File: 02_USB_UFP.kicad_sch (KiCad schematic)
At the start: 36 parts, among them J1 USB_C_Receptacle, U5 TVS2200DRVx, U6 PI3USB302-Ax, U7 TUSB522Px

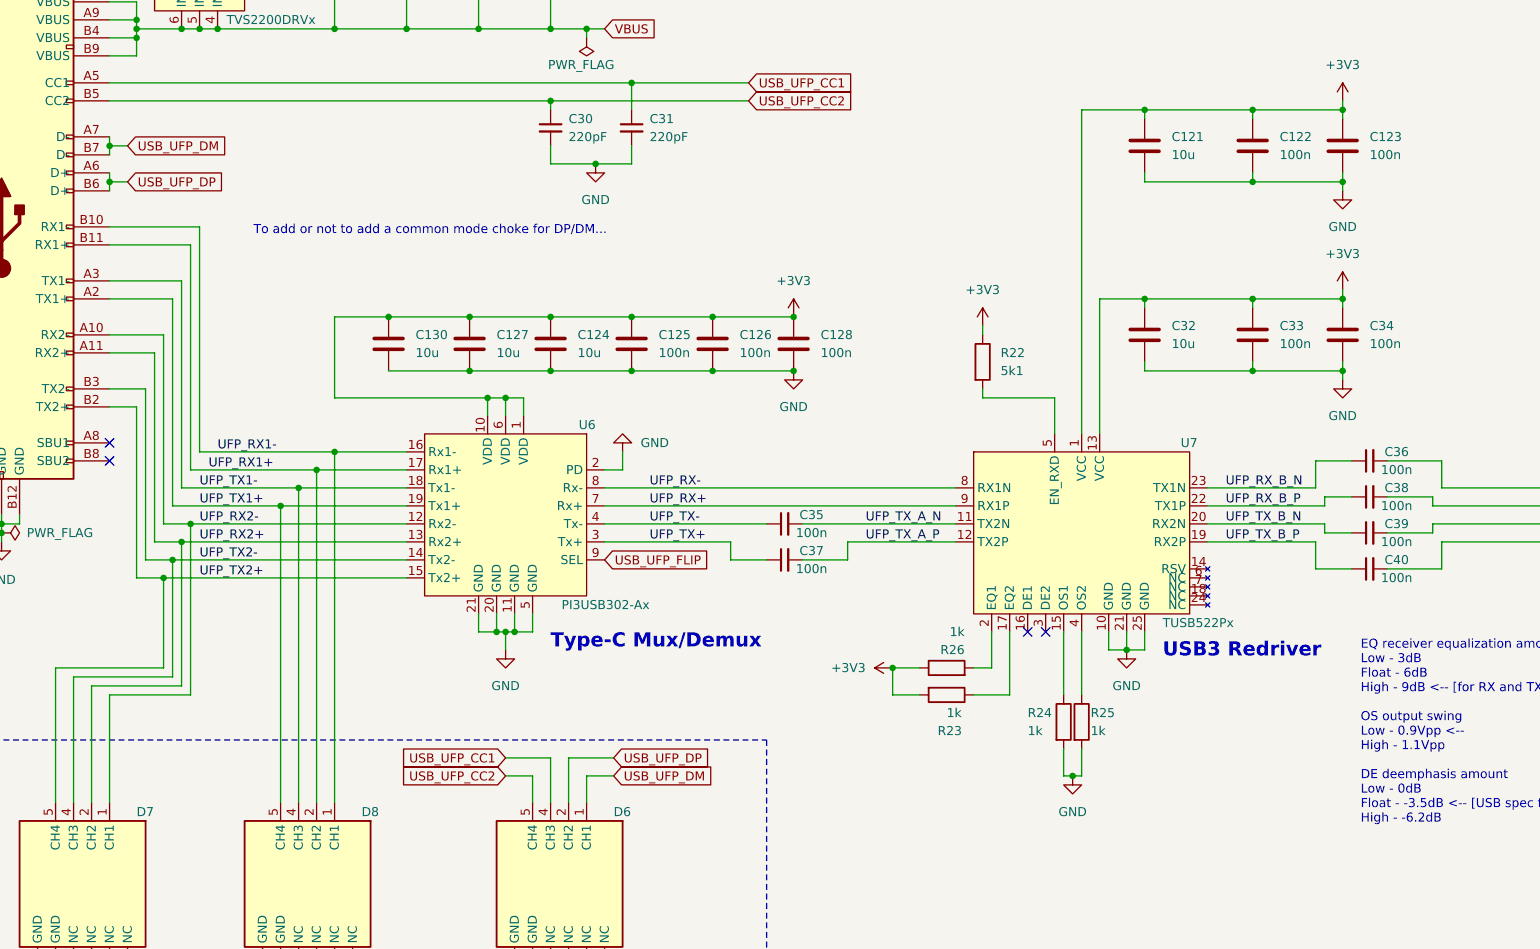
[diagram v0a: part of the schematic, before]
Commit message: route power delivery controller
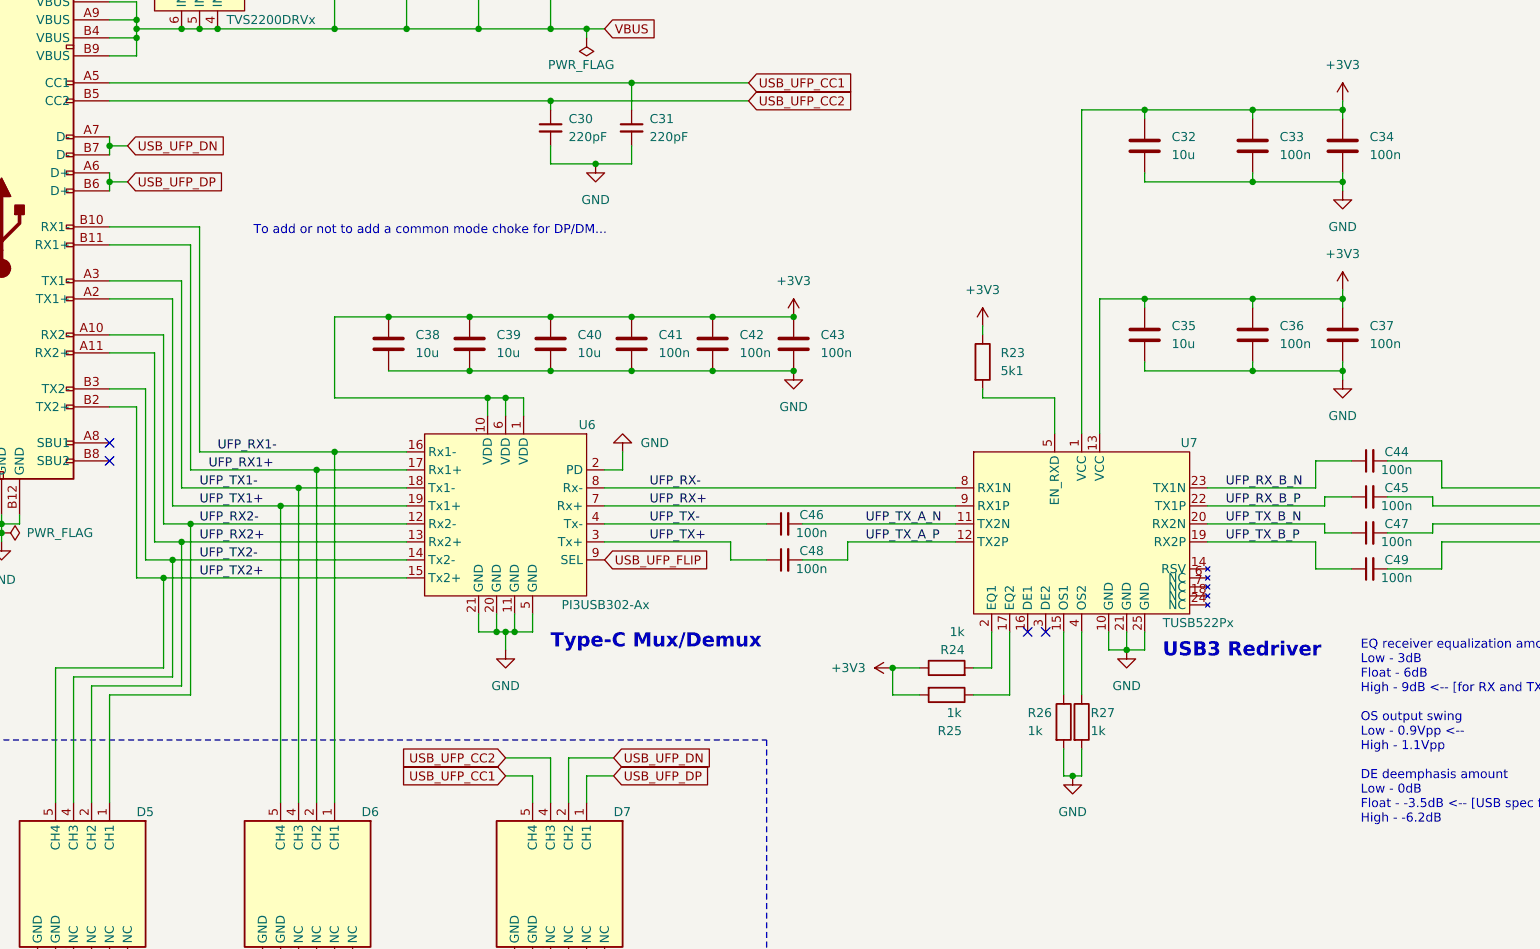
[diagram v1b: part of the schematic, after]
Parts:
- C26, C27, C28, C29: footprint Capacitor_SMD:C_0603_1608Metric -> Capacitor_SMD:C_0402_1005Metric
- renumbered C121 to C32, C122 to C33, C123 to C34, C32 to C35, C33 to C36, C34 to C37, C130 to C38, C127 to C39, C124 to C40, C125 to C41, C126 to C42, C128 to C43, C36 to C44, C38 to C45, C35 to C46, C39 to C47, C37 to C48, C40 to C49, D7 to D5, D8 to D6, D6 to D7, R22 to R23, R26 to R24, R23 to R25, R24 to R26, R25 to R27
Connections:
- net USB_UFP_CC1: now also D7.5 (CH4); no longer D7.4 (CH3)
- net USB_UFP_CC2: now also D7.4 (CH3); no longer D7.5 (CH4)
- net USB_UFP_DP: now also D7.1 (CH1); no longer D7.2 (CH2)
- net USB_UFP_DM renamed USB_UFP_DN
- net USB_UFP_DN: now also D7.2 (CH2); no longer D7.1 (CH1)

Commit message: settle on a layout
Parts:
- C30, C31, C33, C34, C36, C37, C41, C42, C43: footprint Capacitor_SMD:C_0603_1608Metric -> Capacitor_SMD:C_0402_1005Metric
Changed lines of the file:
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@@
       (effects (font (size 1.27 1.27)) (justify left))
     )
-    (property "Footprint" "Capacitor_SMD:C_0603_1608Metric" (at 152.0952 99.06 0)
+    (property "Footprint" "Capacitor_SMD:C_0402_1005Metric" (at 152.0952 99.06 0)
       (effects (font (size 1.27 1.27)) hide)
     )
@@
       (effects (font (size 1.27 1.27)) (justify left))
     )
-    (property "Footprint" "Capacitor_SMD:C_0603_1608Metric" (at 140.6652 99.06 0)
+    (property "Footprint" "Capacitor_SMD:C_0402_1005Metric" (at 140.6652 99.06 0)
       (effects (font (size 1.27 1.27)) hide)
     )
@@
       (effects (font (size 1.27 1.27)) (justify left))
     )
-    (property "Footprint" "Capacitor_SMD:C_0603_1608Metric" (at 216.8652 97.79 0)
+    (property "Footprint" "Capacitor_SMD:C_0402_1005Metric" (at 216.8652 97.79 0)
       (effects (font (size 1.27 1.27)) hide)
     )
@@
       (effects (font (size 1.27 1.27)) (justify left))
     )
-    (property "Footprint" "Capacitor_SMD:C_0603_1608Metric" (at 229.5652 71.12 0)
+    (property "Footprint" "Capacitor_SMD:C_0402_1005Metric" (at 229.5652 71.12 0)
       (effects (font (size 1.27 1.27)) hide)
     )
@@
       (effects (font (size 1.27 1.27)) (justify left))
     )
-    (property "Footprint" "Capacitor_SMD:C_0603_1608Metric" (at 216.8652 71.12 0)
+    (property "Footprint" "Capacitor_SMD:C_0402_1005Metric" (at 216.8652 71.12 0)
       (effects (font (size 1.27 1.27)) hide)
     )
@@
       (effects (font (size 1.27 1.27)) (justify left))
     )
-    (property "Footprint" "Capacitor_SMD:C_0603_1608Metric" (at 129.2352 99.06 0)
+    (property "Footprint" "Capacitor_SMD:C_0402_1005Metric" (at 129.2352 99.06 0)
       (effects (font (size 1.27 1.27)) hide)
     )
@@
       (effects (font (size 1.27 1.27)) (justify left))
     )
-    (property "Footprint" "Capacitor_SMD:C_0603_1608Metric" (at 128.27 64.77 0)
+    (property "Footprint" "Capacitor_SMD:C_0402_1005Metric" (at 128.27 64.77 0)
       (effects (font (size 1.27 1.27)) hide)
     )
@@
       (effects (font (size 1.27 1.27)) (justify left))
     )
-    (property "Footprint" "Capacitor_SMD:C_0603_1608Metric" (at 116.84 64.77 0)
+    (property "Footprint" "Capacitor_SMD:C_0402_1005Metric" (at 116.84 64.77 0)
       (effects (font (size 1.27 1.27)) hide)
     )
@@
       (effects (font (size 1.27 1.27)) (justify left))
     )
-    (property "Footprint" "Capacitor_SMD:C_0603_1608Metric" (at 229.5652 97.79 0)
-      (effects (font (size 1.27 1.27)) hide)
-    )
+    (property "Footprint" "Capacitor_SMD:C_0402_1005Metric" (at 229.5652 97.79 0)
+      (effects (font (size 1.27 1.27)) hide)
+    )

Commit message: fix bom
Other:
- note added: "Hmmm... https://electronics.stackexchange.com/questions/290777/usb-3-0-hub-shield-connection To me, it should be the most upstream (battery side) board that connects the shield to GND via some parallel LC connection"
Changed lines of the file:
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@@
   (junction (at 69.85 50.8) (diameter 0) (color 0 0 0 0)
   )
+  (no_connect (at 31.75 119.38))
   (no_connect (at 54.61 109.22))
   (no_connect (at 186.69 135.89))
   (no_connect (at 184.15 135.89))
-  (no_connect (at 31.75 119.38))
   (no_connect (at 54.61 111.76))
   (wire (pts (xy 189.23 156.21) (xy 190.5 156.21))
@@
     (effects (font (size 2 2) (thickness 0.4) bold) (justify left bottom))
   )
+  (text "Hmmm...\nhttps://electronics.stackexchange.com/questions/290777/usb-3-0-hub-shield-connection\n\nTo me, it should be the most upstream (battery side) board that connects the shield to GND via some parallel LC \nconnection"
+    (at -115.57 132.08 0)
+    (effects (font (size 1.27 1.27)) (justify left bottom))
+  )
   (text "Should I add 2.2Ohm R_ESD and the caps for the RX lines?\n\"An ESD clamp voltage >4V may require a R_ESD on each differential pin, \nwhich should be placed near the USB connector.\""
